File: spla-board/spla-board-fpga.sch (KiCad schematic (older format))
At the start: 42 parts, among them J2 J_JTAG, U1 LFE5U-45F-BG256

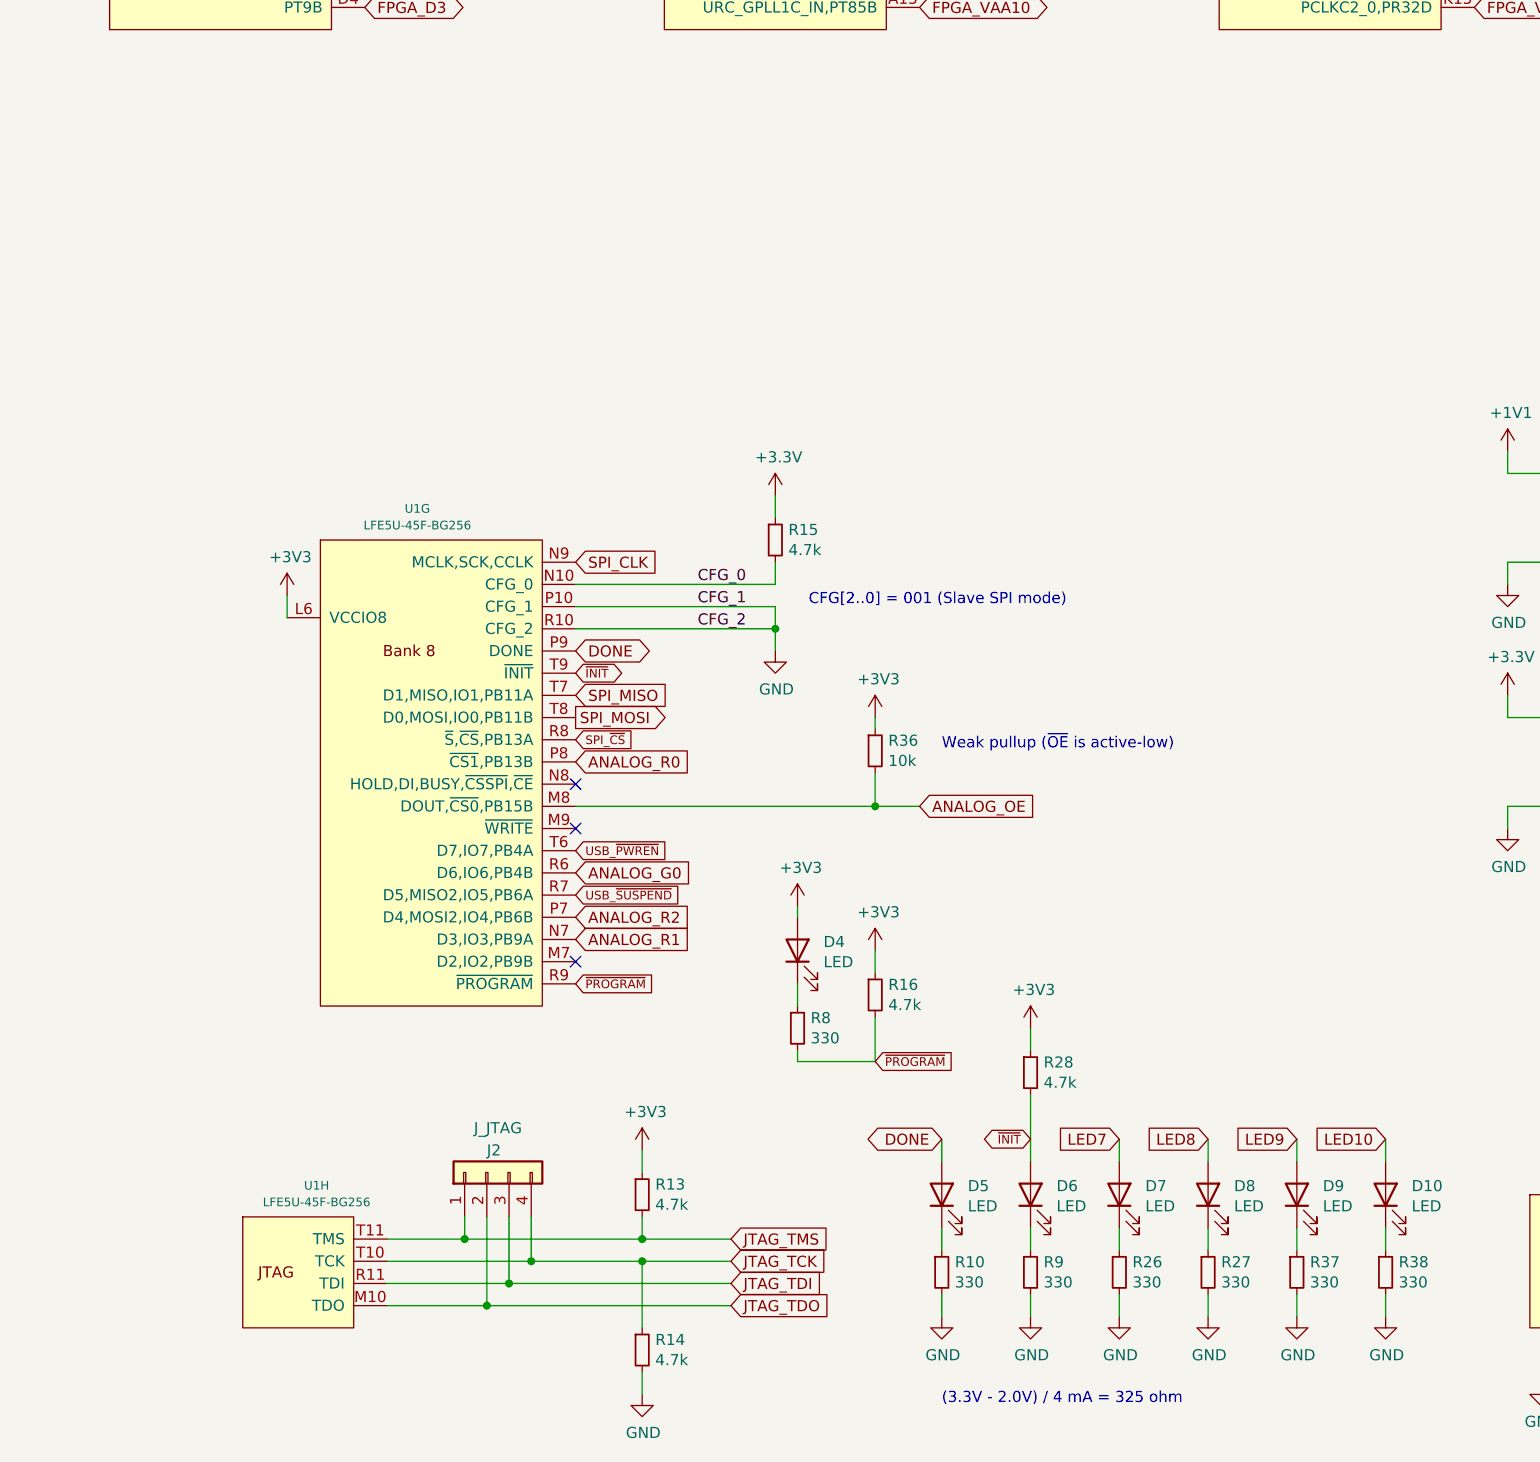
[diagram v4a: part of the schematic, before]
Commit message: schematic/pcb: Add 74LVC1G17 buffers for LEDs; arrange layout to suit.
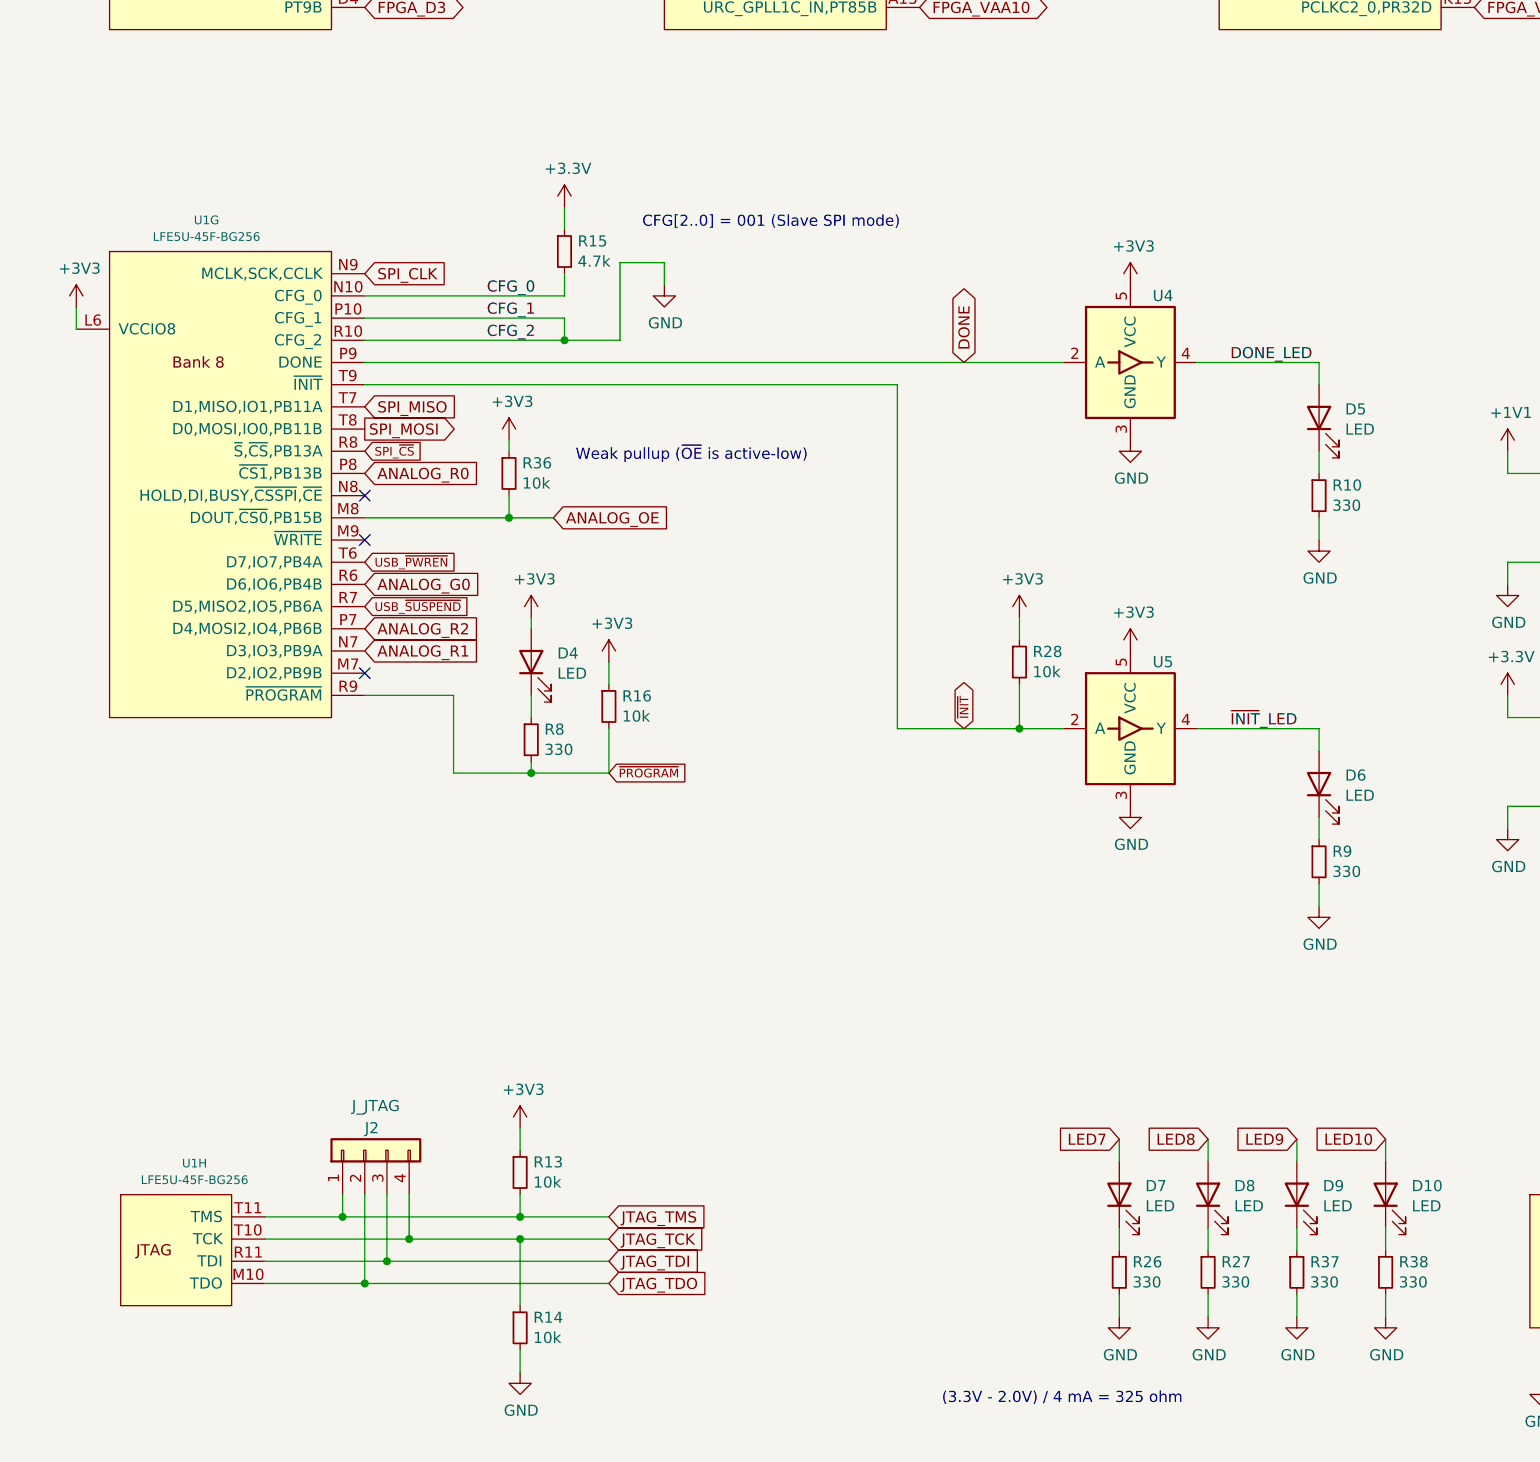
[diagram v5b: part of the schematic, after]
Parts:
- added U4, U5: 74LVC1G17, Package_TO_SOT_SMD:SOT-353_SC-70-5, symbol SPLA:74LVC1G17
- R13, R14, R16, R28: value 4.7k -> 10k; Digikey RMCF0603JT4K70CT-ND -> RMCF0603JT10K0CT-ND; Manufacturer Id RMCF0603JT4K70 -> RMCF0603JT10K0
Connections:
- net +3V3: now also U4.5 (VCC), U5.5 (VCC)
- net DONE: now also U4.2 (A); no longer D5.2 (A)
- net GND: now also U4.3 (GND), U5.3 (GND)
- net ~INIT: now also U5.2 (A); no longer D6.2 (A)
- new net DONE_LED: D5.2 (A), U4.4 (Y)
- new net ~INIT~_LED: D6.2 (A), U5.4 (Y)
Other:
- moved on the sheet: D4, D5, D6, J2, R10, R13, R14, R15, R16, R28, R36, R8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
